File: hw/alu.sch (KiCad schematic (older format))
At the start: 6 parts, among them U701 74HC181, U702 74HC181, U703 74HC182, U704 74HC541, U705 74HC175

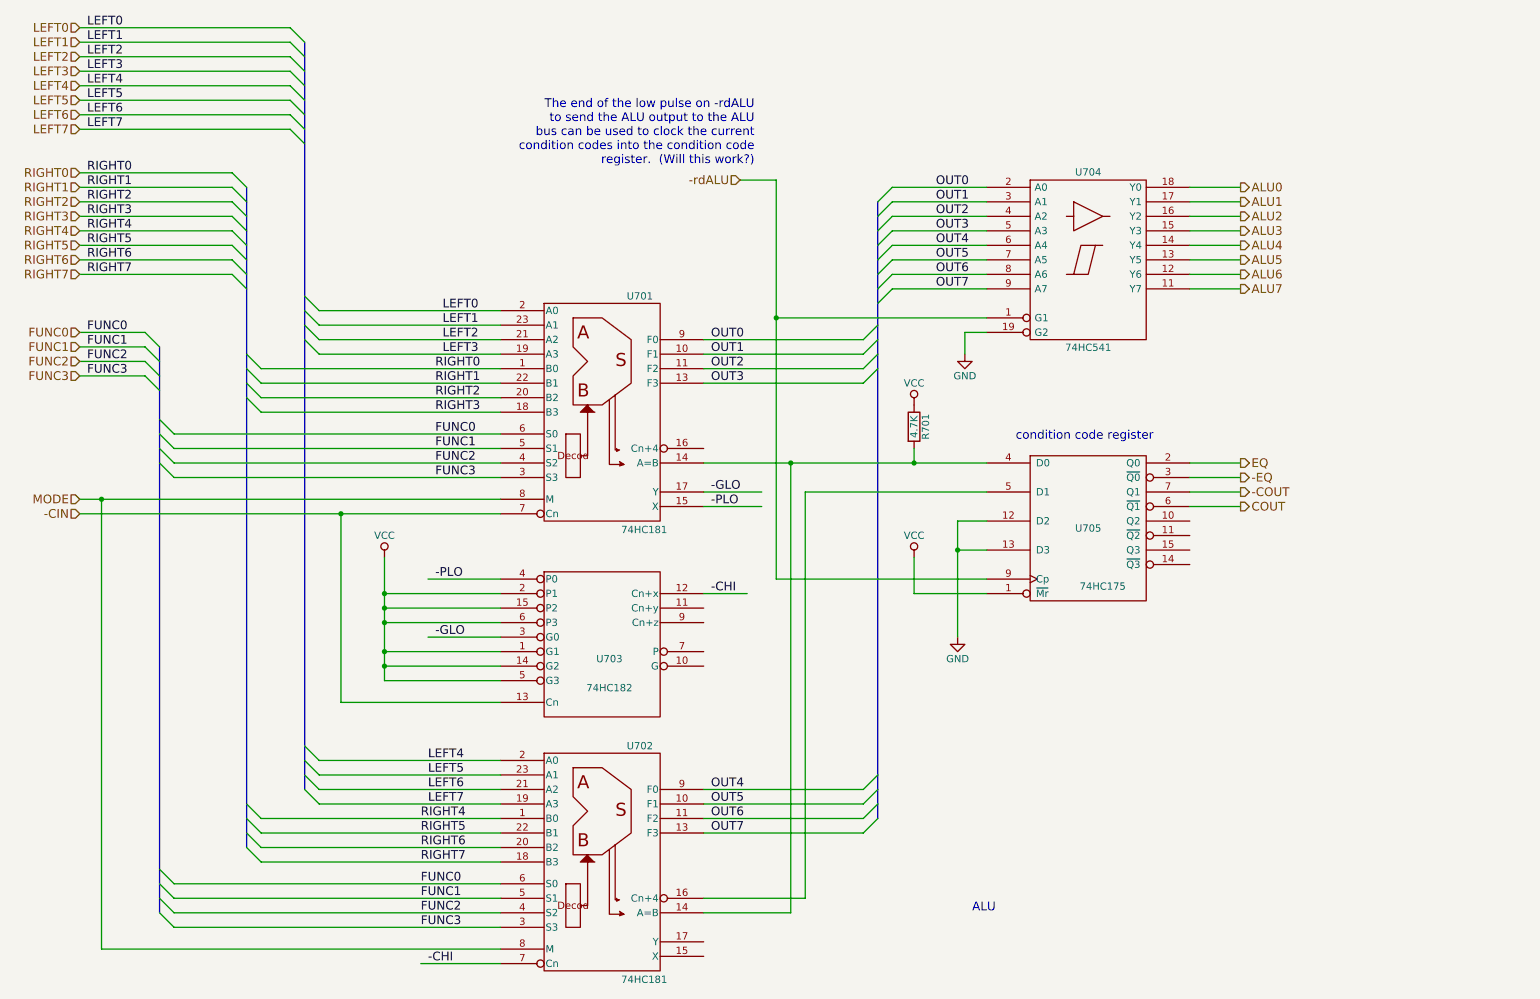
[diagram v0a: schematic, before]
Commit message: add explicit signal to latch condition codes
Was able to use microcode bits more efficiently (to make
room for the new signal) by putting the combinational
logic to generate the external read/write signals after
the '175 microcode signal registers.  This should be fine
as long as memDir is set appropriately before the extRW
signal is asserted.  (No glitches should be possible.)
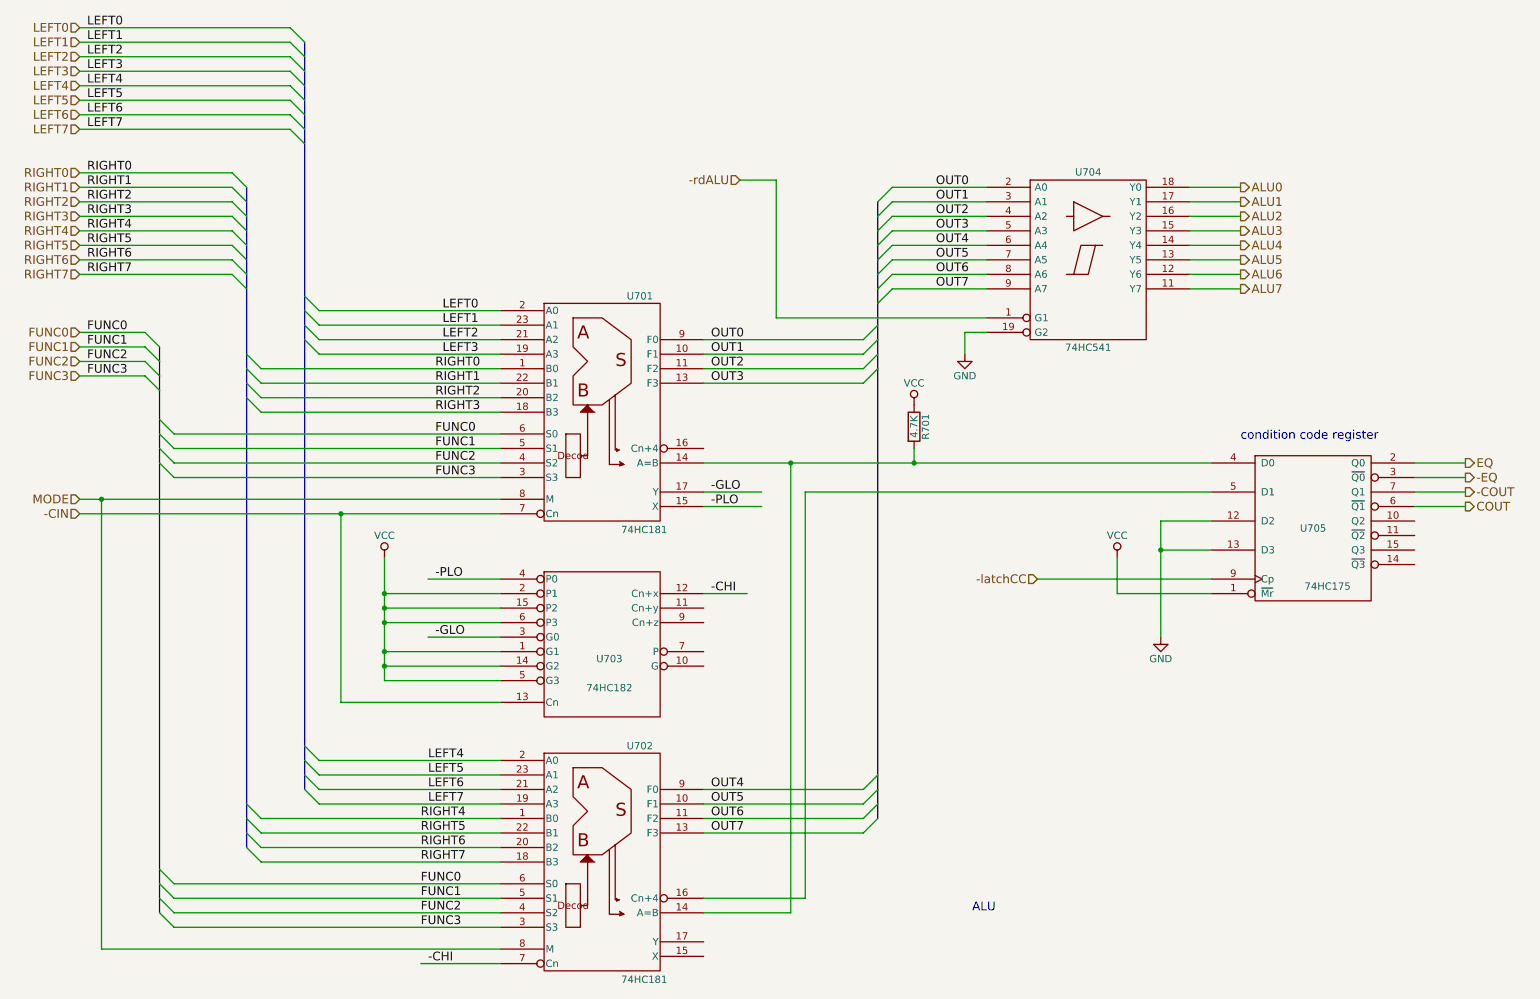
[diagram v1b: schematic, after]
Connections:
- net labels added: -latchCC
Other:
- note removed: "The end of the low pulse on -rdALU\nto send the ALU output to the ALU\nbus can be used to clock the current\ncondition codes into the condition code\nregister. (Will this work?)"
- moved on the sheet: U705
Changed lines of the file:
@@
 	1    0    0    -1
 $EndComp
-Text Notes 7450 3500 0    60   ~ 0
+Text Notes 9000 3500 0    60   ~ 0
 condition code register
-Text Notes 5650 1600 2    60   ~ 0
-The end of the low pulse on -rdALU\nto send the ALU output to the ALU\nbus can be used to clock the current\ncondition codes into the condition code\nregister.  (Will this work?)
 Wire Wire Line
 	1000 650  2450 650
@@
 	7250 2650 5800 2650
 Wire Wire Line
-	5800 1700 5800 4450
-Wire Wire Line
 	5800 1700 5550 1700
 Wire Wire Line
@@
 	8650 2450 9000 2450
 Wire Wire Line
-	5300 3650 7250 3650
+	5300 3650 8800 3650
 Wire Wire Line
 	5300 6750 5900 6750
@@
 	6000 6650 6000 3850
 Wire Wire Line
-	6000 3850 7250 3850
-Wire Wire Line
-	5800 4450 7250 4450
-Connection ~ 5800 2650
-Wire Wire Line
-	8650 3650 9000 3650
-Wire Wire Line
-	8650 3850 9000 3850
-Text HLabel 9000 3650 2    60   Output ~ 0
+	6000 3850 8800 3850
+Wire Wire Line
+	10200 3650 10550 3650
+Wire Wire Line
+	10200 3850 10550 3850
+Text HLabel 10550 3650 2    60   Output ~ 0
 EQ
-Text HLabel 9000 3850 2    60   Output ~ 0
+Text HLabel 10550 3850 2    60   Output ~ 0
 -COUT
 Wire Wire Line
@@
 L 74LS175 U705
 U 1 1 594A6E0F
-P 7950 4100
-F 0 "U705" H 7950 4100 50  0000 C CNN
-F 1 "74HC175" H 8050 3700 50  0000 C CNN
-F 2 "" H 7950 4100 50  0001 C CNN
-F 3 "" H 7950 4100 50  0001 C CNN
-	1    7950 4100
-	1    0    0    -1
-$EndComp
-Wire Wire Line
-	7250 4050 7050 4050
-Wire Wire Line
-	7050 4050 7050 4850
-Wire Wire Line
-	7250 4250 7050 4250
-Connection ~ 7050 4250
+P 9500 4100
+F 0 "U705" H 9500 4100 50  0000 C CNN
+F 1 "74HC175" H 9600 3700 50  0000 C CNN
+F 2 "" H 9500 4100 50  0001 C CNN
+F 3 "" H 9500 4100 50  0001 C CNN
+	1    9500 4100
+	1    0    0    -1
+$EndComp
+Wire Wire Line
+	8800 4050 8450 4050
+Wire Wire Line
+	8450 4050 8450 4850
+Wire Wire Line
+	8800 4250 8450 4250
+Connection ~ 8450 4250
 $Comp
 L GND #PWR?
 U 1 1 594A7340
-P 7050 4850
-F 0 "#PWR?" H 7050 4600 50  0001 C CNN
-F 1 "GND" H 7050 4700 50  0000 C CNN
-F 2 "" H 7050 4850 50  0001 C CNN
-F 3 "" H 7050 4850 50  0001 C CNN
-	1    7050 4850
-	1    0    0    -1
-$EndComp
-Wire Wire Line
-	7250 4550 6750 4550
-Wire Wire Line
-	6750 4550 6750 4300
+P 8450 4850
+F 0 "#PWR?" H 8450 4600 50  0001 C CNN
+F 1 "GND" H 8450 4700 50  0000 C CNN
+F 2 "" H 8450 4850 50  0001 C CNN
+F 3 "" H 8450 4850 50  0001 C CNN
+	1    8450 4850
+	1    0    0    -1
+$EndComp
+Wire Wire Line
+	8800 4550 8150 4550
+Wire Wire Line
+	8150 4550 8150 4300
 $Comp
 L VCC #PWR?
 U 1 1 594A7432
-P 6750 4300
-F 0 "#PWR?" H 6750 4150 50  0001 C CNN
-F 1 "VCC" H 6750 4450 50  0000 C CNN
-F 2 "" H 6750 4300 50  0001 C CNN
-F 3 "" H 6750 4300 50  0001 C CNN
-	1    6750 4300
-	1    0    0    -1
-$EndComp
-Wire Wire Line
-	8650 3750 9000 3750
-Wire Wire Line
-	8650 3950 9000 3950
-Text HLabel 9000 3750 2    60   Output ~ 0
+P 8150 4300
+F 0 "#PWR?" H 8150 4150 50  0001 C CNN
+F 1 "VCC" H 8150 4450 50  0000 C CNN
+F 2 "" H 8150 4300 50  0001 C CNN
+F 3 "" H 8150 4300 50  0001 C CNN
+	1    8150 4300
+	1    0    0    -1
+$EndComp
+Wire Wire Line
+	10200 3750 10550 3750
+Wire Wire Line
+	10200 3950 10550 3950
+Text HLabel 10550 3750 2    60   Output ~ 0
 -EQ
-Text HLabel 9000 3950 2    60   Output ~ 0
+Text HLabel 10550 3950 2    60   Output ~ 0
 COUT
+Wire Wire Line
+	5800 2650 5800 1700
+Text HLabel 7600 4450 0    60   Input ~ 0
+-latchCC
+Wire Wire Line
+	7600 4450 8800 4450
 $EndSCHEMATC

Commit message: tweaks to ALU schematic for readability
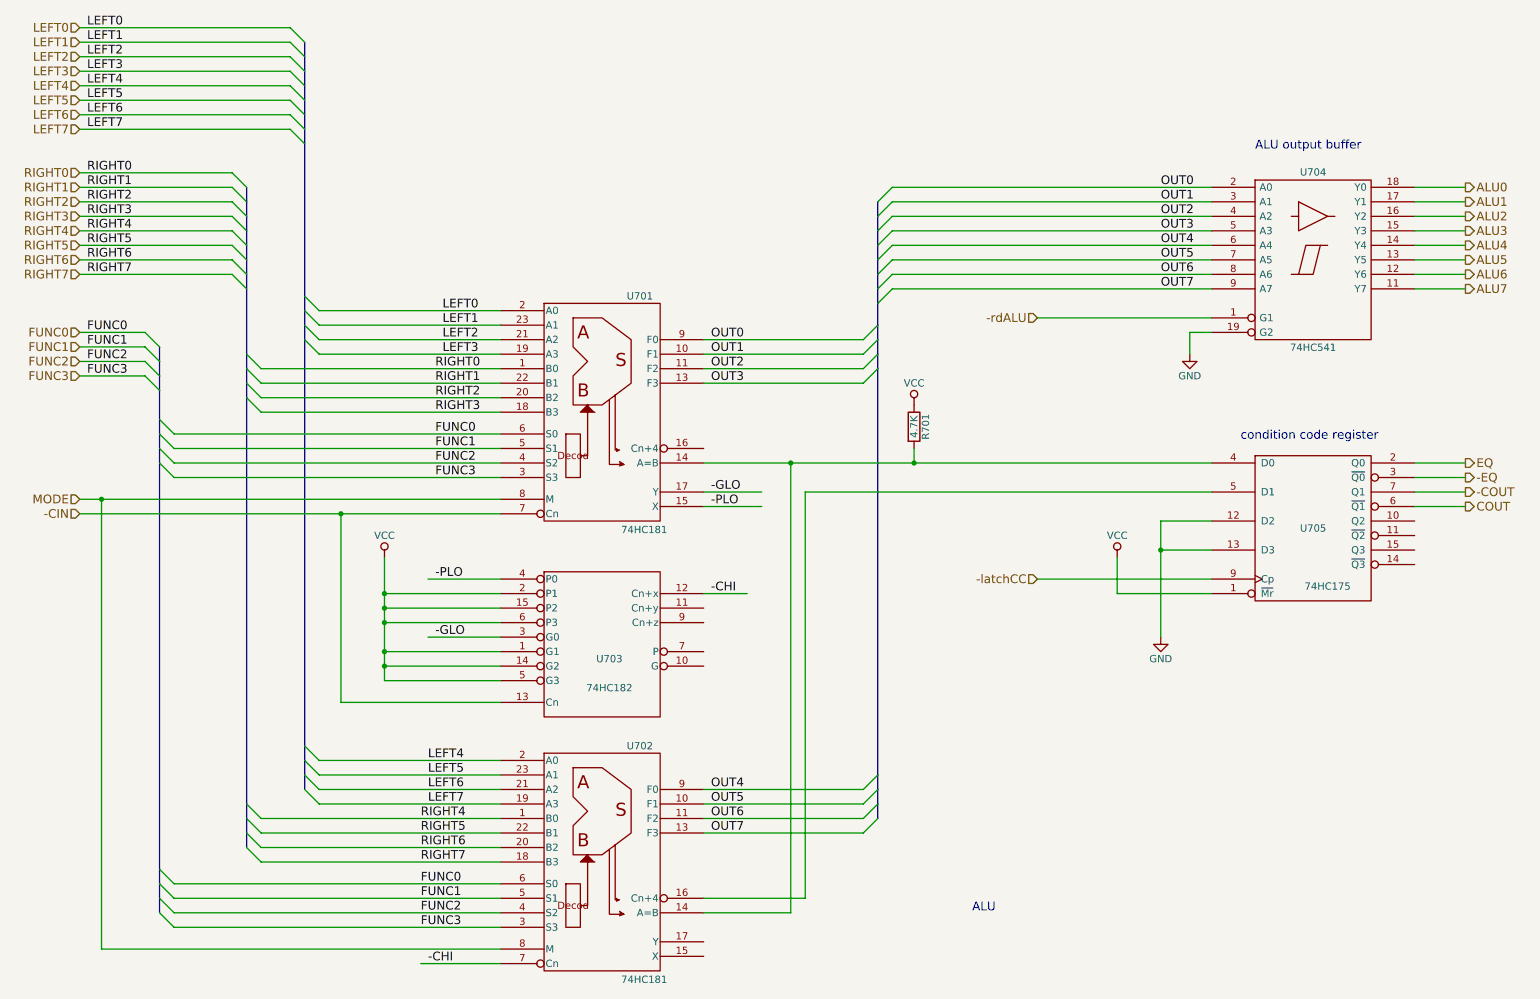
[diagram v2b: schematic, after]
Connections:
- wire segments 109 -> 117
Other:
- note added: "ALU output buffer"
- moved on the sheet: U704
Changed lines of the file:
@@
 Entry Wire Line
 	6500 2550 6600 2450
-Text Label 6900 1750 0    60   ~ 0
+Text Label 8450 1750 0    60   ~ 0
 OUT0
-Text Label 6900 1850 0    60   ~ 0
+Text Label 8450 1850 0    60   ~ 0
 OUT1
-Text Label 6900 1950 0    60   ~ 0
+Text Label 8450 1950 0    60   ~ 0
 OUT2
-Text Label 6900 2050 0    60   ~ 0
+Text Label 8450 2050 0    60   ~ 0
 OUT3
-Text Label 6900 2150 0    60   ~ 0
+Text Label 8450 2150 0    60   ~ 0
 OUT4
-Text Label 6900 2250 0    60   ~ 0
+Text Label 8450 2250 0    60   ~ 0
 OUT5
-Text Label 6900 2350 0    60   ~ 0
+Text Label 8450 2350 0    60   ~ 0
 OUT6
-Text Label 6900 2450 0    60   ~ 0
+Text Label 8450 2450 0    60   ~ 0
 OUT7
 $Comp
 L 74LS541 U704
 U 1 1 5948525C
-P 7950 2250
-F 0 "U704" H 7950 2825 50  0000 C BNN
-F 1 "74HC541" H 7950 1675 50  0000 C TNN
-F 2 "" H 7950 2250 50  0001 C CNN
-F 3 "" H 7950 2250 50  0001 C CNN
-	1    7950 2250
-	1    0    0    -1
-$EndComp
-Text HLabel 5550 1700 0    60   Input ~ 0
+P 9500 2250
+F 0 "U704" H 9500 2825 50  0000 C BNN
+F 1 "74HC541" H 9500 1675 50  0000 C TNN
+F 2 "" H 9500 2250 50  0001 C CNN
+F 3 "" H 9500 2250 50  0001 C CNN
+	1    9500 2250
+	1    0    0    -1
+$EndComp
+Text HLabel 7600 2650 0    60   Input ~ 0
 -rdALU
 $Comp
 L GND #PWR?
 U 1 1 5948539E
-P 7100 2900
-F 0 "#PWR?" H 7100 2650 50  0001 C CNN
-F 1 "GND" H 7100 2750 50  0000 C CNN
-F 2 "" H 7100 2900 50  0001 C CNN
-F 3 "" H 7100 2900 50  0001 C CNN
-	1    7100 2900
-	1    0    0    -1
-$EndComp
-Text HLabel 9000 1750 2    60   Output ~ 0
+P 8650 2900
+F 0 "#PWR?" H 8650 2650 50  0001 C CNN
+F 1 "GND" H 8650 2750 50  0000 C CNN
+F 2 "" H 8650 2900 50  0001 C CNN
+F 3 "" H 8650 2900 50  0001 C CNN
+	1    8650 2900
+	1    0    0    -1
+$EndComp
+Text HLabel 10550 1750 2    60   Output ~ 0
 ALU0
-Text HLabel 9000 1850 2    60   Output ~ 0
+Text HLabel 10550 1850 2    60   Output ~ 0
 ALU1
-Text HLabel 9000 1950 2    60   Output ~ 0
+Text HLabel 10550 1950 2    60   Output ~ 0
 ALU2
-Text HLabel 9000 2050 2    60   Output ~ 0
+Text HLabel 10550 2050 2    60   Output ~ 0
 ALU3
-Text HLabel 9000 2150 2    60   Output ~ 0
+Text HLabel 10550 2150 2    60   Output ~ 0
 ALU4
-Text HLabel 9000 2250 2    60   Output ~ 0
+Text HLabel 10550 2250 2    60   Output ~ 0
 ALU5
-Text HLabel 9000 2350 2    60   Output ~ 0
+Text HLabel 10550 2350 2    60   Output ~ 0
 ALU6
-Text HLabel 9000 2450 2    60   Output ~ 0
+Text HLabel 10550 2450 2    60   Output ~ 0
 ALU7
 $Comp
@@
 	1000 1350 2450 1350
 Wire Bus Line
-	2550 750  2550 5900
+	2550 750  2550 850
+Wire Bus Line
+	2550 850  2550 950
+Wire Bus Line
+	2550 950  2550 1050
+Wire Bus Line
+	2550 1050 2550 1150
+Wire Bus Line
+	2550 1150 2550 1250
+Wire Bus Line
+	2550 1250 2550 1350
+Wire Bus Line
+	2550 1350 2550 1450
+Wire Bus Line
+	2550 1450 2550 2500
+Wire Bus Line
+	2550 2500 2550 2600
+Wire Bus Line
+	2550 2600 2550 2700
+Wire Bus Line
+	2550 2700 2550 2800
+Wire Bus Line
+	2550 2800 2550 5600
+Wire Bus Line
+	2550 5600 2550 5700
+Wire Bus Line
+	2550 5700 2550 5800
+Wire Bus Line
+	2550 5800 2550 5900
 Wire Wire Line
 	2650 2600 3900 2600
@@
 	1000 2350 2050 2350
 Wire Bus Line
-	2150 1750 2150 6300
+	2150 1750 2150 1850
+Wire Bus Line
+	2150 1850 2150 1950
+Wire Bus Line
+	2150 1950 2150 2050
+Wire Bus Line
+	2150 2050 2150 2150
+Wire Bus Line
+	2150 2150 2150 2250
+Wire Bus Line
+	2150 2250 2150 2350
+Wire Bus Line
+	2150 2350 2150 2450
+Wire Bus Line
+	2150 2450 2150 2900
+Wire Bus Line
+	2150 2900 2150 3000
+Wire Bus Line
+	2150 3000 2150 3100
+Wire Bus Line
+	2150 3100 2150 3200
+Wire Bus Line
+	2150 3200 2150 6000
+Wire Bus Line
+	2150 6000 2150 6100
+Wire Bus Line
+	2150 6100 2150 6200
+Wire Bus Line
+	2150 6200 2150 6300
 Wire Wire Line
 	3900 3000 2250 3000
@@
 	1000 3050 1450 3050
 Wire Bus Line
-	1550 2850 1550 6750
+	1550 2850 1550 2950
+Wire Bus Line
+	1550 2950 1550 3050
+Wire Bus Line
+	1550 3050 1550 3150
+Wire Bus Line
+	1550 3150 1550 3350
+Wire Bus Line
+	1550 3350 1550 3450
+Wire Bus Line
+	1550 3450 1550 3550
+Wire Bus Line
+	1550 3550 1550 3650
+Wire Bus Line
+	1550 3650 1550 6450
+Wire Bus Line
+	1550 6450 1550 6550
+Wire Bus Line
+	1550 6550 1550 6650
+Wire Bus Line
+	1550 6650 1550 6750
 Wire Wire Line
 	3900 3450 1650 3450
@@
 	3900 6850 1650 6850
 Wire Wire Line
-	1000 3900 3900 3900
-Wire Wire Line
-	1000 4000 3900 4000
+	1000 3900 1150 3900
+Wire Wire Line
+	1150 3900 3900 3900
+Wire Wire Line
+	1000 4000 2800 4000
+Wire Wire Line
+	2800 4000 3900 4000
 Wire Wire Line
 	5300 3850 5700 3850
@@
 	5300 6200 6400 6200
 Wire Bus Line
-	6500 1850 6500 6100
-Wire Wire Line
-	6600 1750 7250 1750
-Wire Wire Line
-	6600 1850 7250 1850
-Wire Wire Line
-	6600 1950 7250 1950
-Wire Wire Line
-	6600 2050 7250 2050
-Wire Wire Line
-	6600 2150 7250 2150
-Wire Wire Line
-	6600 2250 7250 2250
-Wire Wire Line
-	6600 2350 7250 2350
-Wire Wire Line
-	6600 2450 7250 2450
-Wire Wire Line
-	7250 2650 5800 2650
-Wire Wire Line
-	5800 1700 5550 1700
-Wire Wire Line
-	7250 2750 7100 2750
-Wire Wire Line
-	7100 2750 7100 2900
-Wire Wire Line
-	8650 1750 9000 1750
-Wire Wire Line
-	8650 1850 9000 1850
-Wire Wire Line
-	8650 1950 9000 1950
-Wire Wire Line
-	8650 2050 9000 2050
-Wire Wire Line
-	8650 2150 9000 2150
-Wire Wire Line
-	8650 2250 9000 2250
-Wire Wire Line
-	8650 2350 9000 2350
-Wire Wire Line
-	8650 2450 9000 2450
-Wire Wire Line
-	5300 3650 8800 3650
+	6500 1850 6500 1950
+Wire Bus Line
+	6500 1950 6500 2050
+Wire Bus Line
+	6500 2050 6500 2150
+Wire Bus Line
+	6500 2150 6500 2250
+Wire Bus Line
+	6500 2250 6500 2350
+Wire Bus Line
+	6500 2350 6500 2450
+Wire Bus Line
+	6500 2450 6500 2550
+Wire Bus Line
+	6500 2550 6500 2700
+Wire Bus Line
+	6500 2700 6500 2800
+Wire Bus Line
+	6500 2800 6500 2900
+Wire Bus Line
+	6500 2900 6500 3000
+Wire Bus Line
+	6500 3000 6500 5800
+Wire Bus Line
+	6500 5800 6500 5900
+Wire Bus Line
+	6500 5900 6500 6000
+Wire Bus Line
+	6500 6000 6500 6100
+Wire Wire Line
+	6600 1750 8800 1750
+Wire Wire Line
+	6600 1850 8800 1850
+Wire Wire Line
+	6600 1950 8800 1950
+Wire Wire Line
+	6600 2050 8800 2050
+Wire Wire Line
+	6600 2150 8800 2150
+Wire Wire Line
+	6600 2250 8800 2250
+Wire Wire Line
+	6600 2350 8800 2350
+Wire Wire Line
+	6600 2450 8800 2450
+Wire Wire Line
+	8800 2650 7600 2650
+Wire Wire Line
+	8800 2750 8650 2750
+Wire Wire Line
+	8650 2750 8650 2900
+Wire Wire Line
+	10200 1750 10550 1750
+Wire Wire Line
+	10200 1850 10550 1850
+Wire Wire Line
+	10200 1950 10550 1950
+Wire Wire Line
+	10200 2050 10550 2050
+Wire Wire Line
+	10200 2150 10550 2150
+Wire Wire Line
+	10200 2250 10550 2250
+Wire Wire Line
+	10200 2350 10550 2350
+Wire Wire Line
+	10200 2450 10550 2450
+Wire Wire Line
+	5300 3650 5900 3650
+Wire Wire Line
+	5900 3650 6750 3650
+Wire Wire Line
+	6750 3650 8800 3650
 Wire Wire Line
 	5300 6750 5900 6750
@@
 -COUT
 Wire Wire Line
-	3100 4300 3100 5150
+	3100 4300 3100 4550
+Wire Wire Line
+	3100 4550 3100 4650
+Wire Wire Line
+	3100 4650 3100 4750
+Wire Wire Line
+	3100 4750 3100 4950
+Wire Wire Line
+	3100 4950 3100 5050
+Wire Wire Line
+	3100 5050 3100 5150
 Wire Wire Line
 	2800 5300 2800 4000
@@
 	8800 4050 8450 4050
 Wire Wire Line
-	8450 4050 8450 4850
+	8450 4050 8450 4250
+Wire Wire Line
+	8450 4250 8450 4850
 Wire Wire Line
 	8800 4250 8450 4250
@@
 Text HLabel 10550 3950 2    60   Output ~ 0
 COUT
-Wire Wire Line
-	5800 2650 5800 1700
 Text HLabel 7600 4450 0    60   Input ~ 0
 -latchCC
 Wire Wire Line
 	7600 4450 8800 4450
+Text Notes 9100 1500 0    60   ~ 0
+ALU output buffer
 $EndSCHEMATC
